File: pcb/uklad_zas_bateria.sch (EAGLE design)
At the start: 32 parts

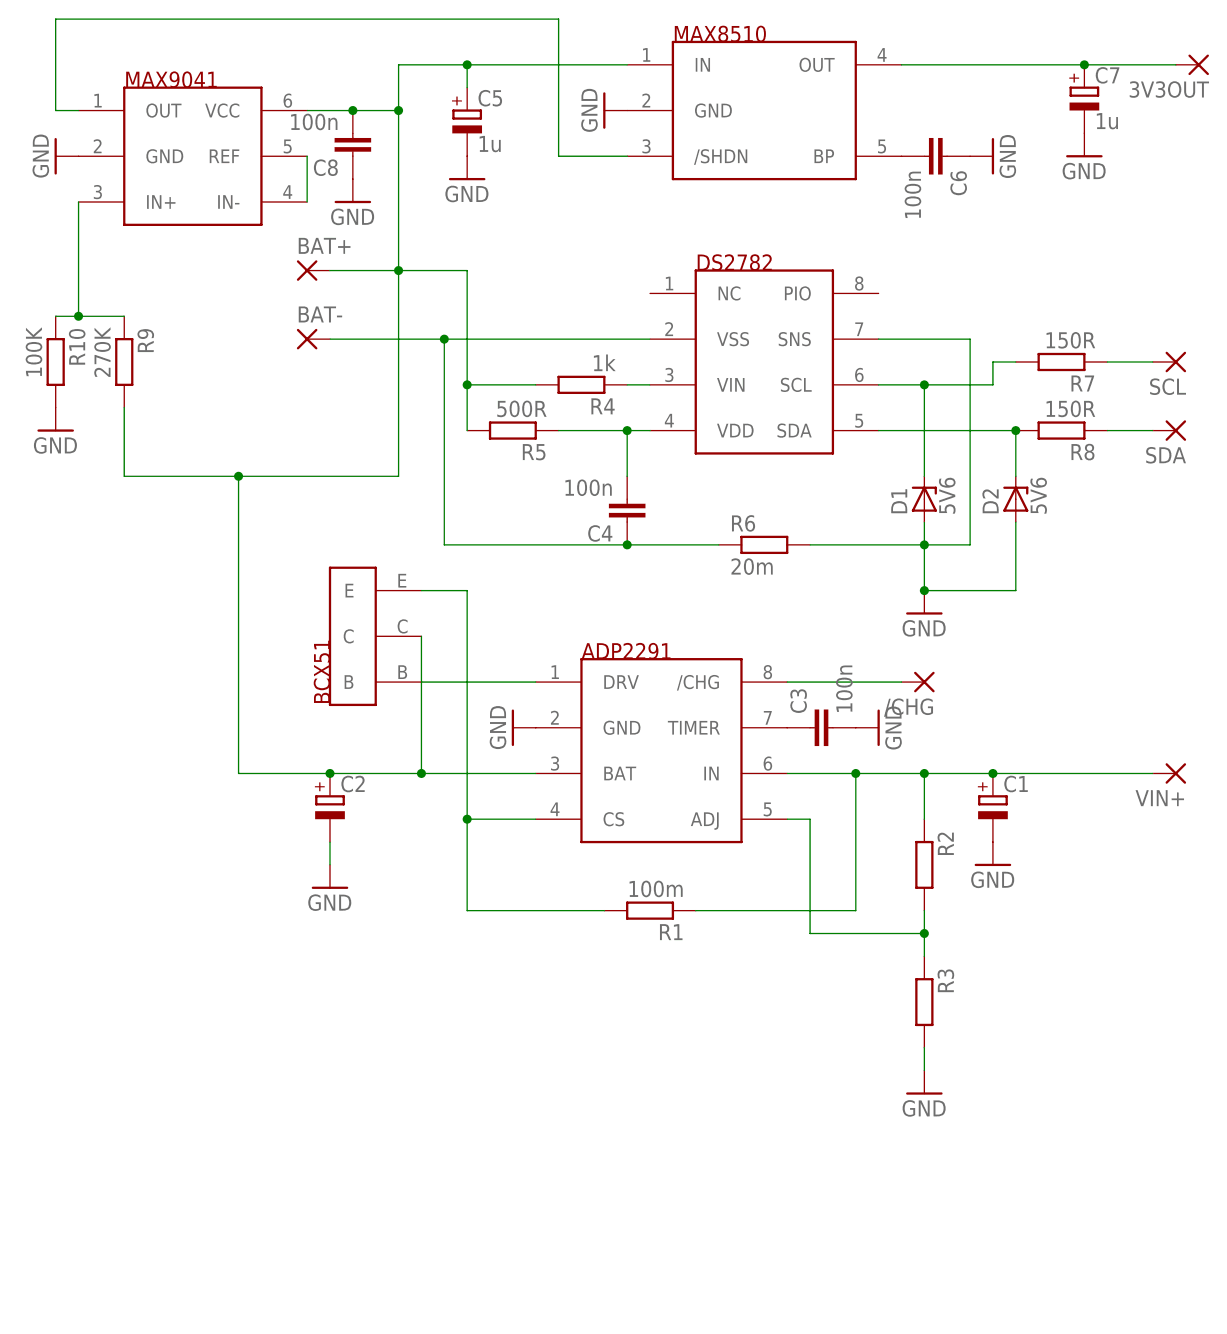
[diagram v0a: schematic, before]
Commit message: dodanie worda z magisterką gdzie pisze na bierząco, update kosztorysu, nowe bordy
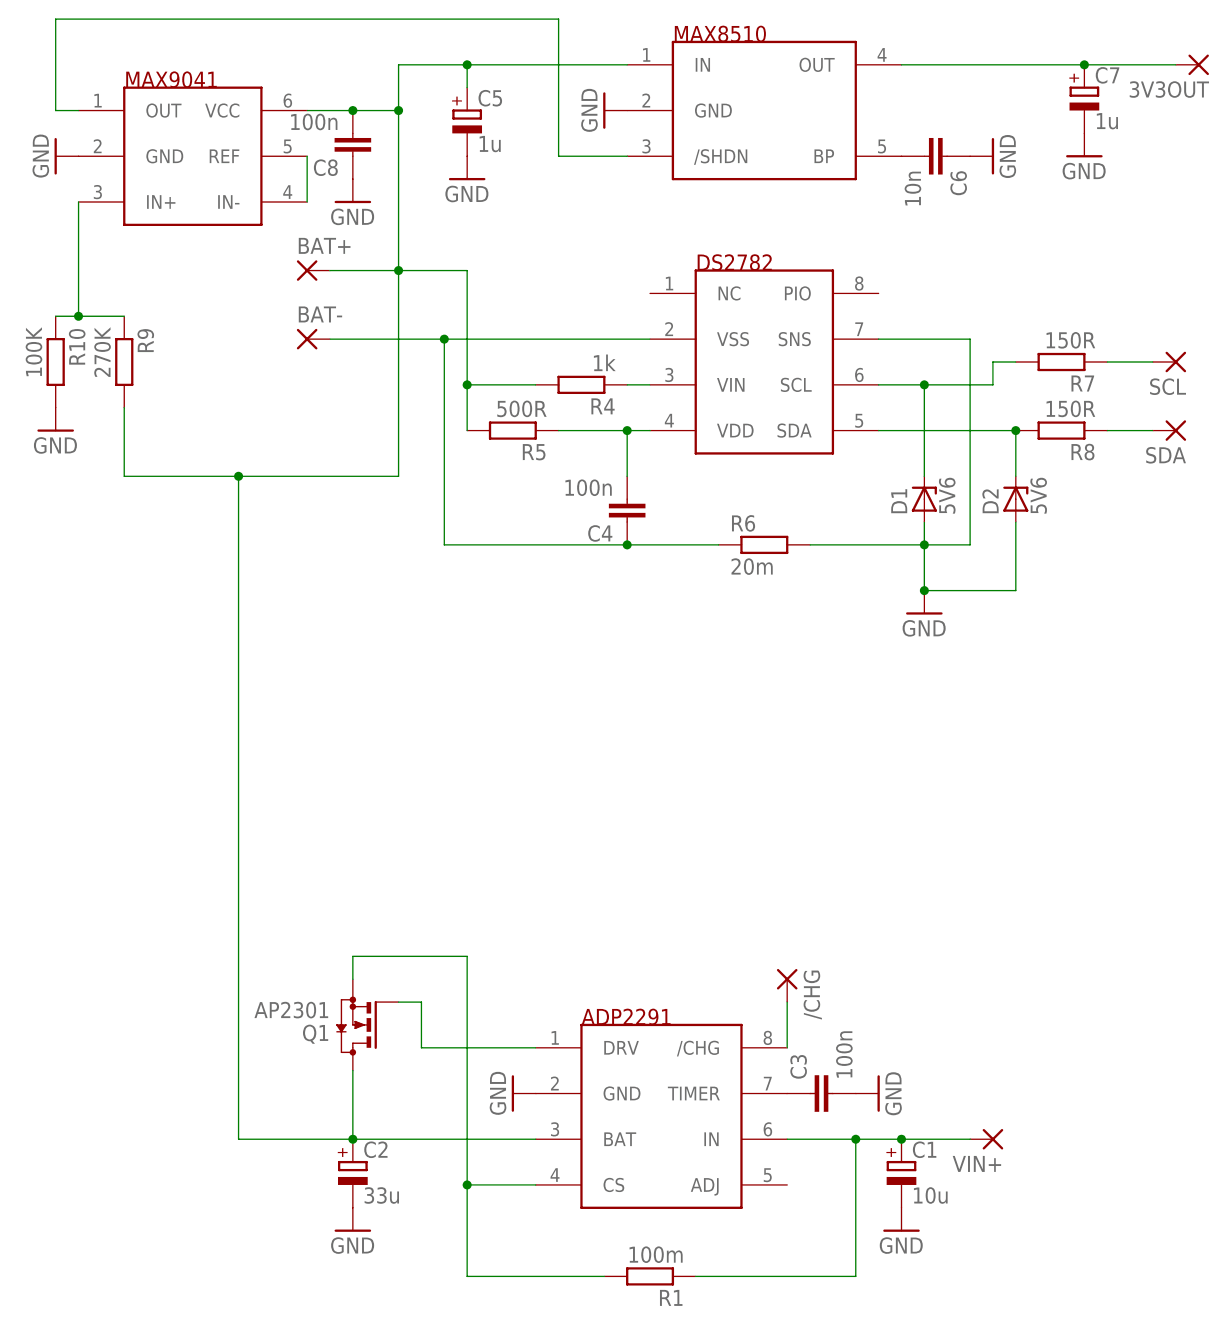
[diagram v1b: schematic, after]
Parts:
- removed R2, R3: (no value), resistor:R-EU_M0805
- removed U$2: BCX51, ref-packages:BCX51
- added Q1: AP2301, transistor-small-signal:BSS123
- C1: value (none) -> 10u
- C2: value (none) -> 33u
- C6: value 100n -> 10n; device rcl:C-EUC0805 -> rcl:C-EUC0603
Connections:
- removed net N$7: R2.2, R3.1, U$1.ADJ
- net GND: no longer R3.2
- net N$1: now also Q1.G; no longer U$2.B
- net N$19: now also Q1.D; no longer U$2.C
- net N$2: now also Q1.S; no longer U$2.E
- net N$3: no longer R2.1
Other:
- moved on the sheet: /CHG, C1, C2, C3, R1, VIN+
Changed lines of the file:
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@@
 <parts>
 <part name="U$1" library="ref-packages" deviceset="ADP2291" device=""/>
-<part name="U$2" library="ref-packages" deviceset="BCX51" device=""/>
 <part name="R1" library="rcl" deviceset="R-EU_" device="0207/10" value="100m"/>
-<part name="C1" library="rcl" deviceset="CPOL-EU" device="E2-5"/>
-<part name="C2" library="rcl" deviceset="CPOL-EU" device="E2-5"/>
+<part name="C1" library="rcl" deviceset="CPOL-EU" device="E2-5" value="10u"/>
+<part name="C2" library="rcl" deviceset="CPOL-EU" device="E2-5" value="33u"/>
 <part name="GND1" library="supply1" deviceset="GND" device=""/>
 <part name="GND2" library="supply1" deviceset="GND" device=""/>
 <part name="GND4" library="supply1" deviceset="GND" device=""/>
-<part name="R2" library="resistor" deviceset="R-EU_" device="M0805"/>
-<part name="R3" library="resistor" deviceset="R-EU_" device="M0805"/>
-<part name="GND3" library="supply1" deviceset="GND" device=""/>
 <part name="/CHG" library="wirepad" deviceset="2,54/0,8" device=""/>
 <part name="C3" library="rcl" deviceset="C-EU" device="C0805" value="100n"/>
@@
 <part name="C7" library="rcl" deviceset="CPOL-EU" device="E2-5" value="1u"/>
 <part name="GND10" library="supply1" deviceset="GND" device=""/>
-<part name="C6" library="rcl" deviceset="C-EU" device="C0805" value="100n"/>
+<part name="C6" library="rcl" deviceset="C-EU" device="C0603" value="10n"/>
 <part name="U$5" library="ref-packages" deviceset="MAX9041" device=""/>
 <part name="GND11" library="supply1" deviceset="GND" device=""/>
@@
 <part name="C8" library="rcl" deviceset="C-EU" device="C0805" value="100n"/>
 <part name="GND13" library="supply1" deviceset="GND" device=""/>
+<part name="Q1" library="transistor-small-signal" deviceset="BSS123" device="" value="AP2301"/>
 </parts>
 <sheets>
@@
 </plain>
 <instances>
-<instance part="U$1" gate="G$1" x="-81.28" y="27.94"/>
-<instance part="U$2" gate="G$1" x="-114.3" y="40.64" rot="R90"/>
-<instance part="R1" gate="G$1" x="-81.28" y="10.16" rot="R180"/>
-<instance part="C1" gate="G$1" x="-43.18" y="22.86"/>
-<instance part="C2" gate="G$1" x="-116.84" y="22.86"/>
-<instance part="GND1" gate="1" x="-116.84" y="12.7"/>
-<instance part="GND2" gate="1" x="-43.18" y="15.24"/>
-<instance part="GND4" gate="1" x="-96.52" y="30.48" rot="R270"/>
-<instance part="R2" gate="G$1" x="-50.8" y="15.24" rot="R270"/>
-<instance part="R3" gate="G$1" x="-50.8" y="0" rot="R270"/>
-<instance part="GND3" gate="1" x="-50.8" y="-10.16"/>
-<instance part="/CHG" gate="P" x="-50.8" y="35.56" rot="R180"/>
-<instance part="C3" gate="G$1" x="-63.5" y="30.48" rot="R90"/>
-<instance part="GND5" gate="1" x="-55.88" y="30.48" rot="R90"/>
-<instance part="VIN+" gate="P" x="-22.86" y="25.4" rot="R180"/>
+<instance part="U$1" gate="G$1" x="-81.28" y="-12.7"/>
+<instance part="R1" gate="G$1" x="-81.28" y="-30.48" rot="R180"/>
+<instance part="C1" gate="G$1" x="-53.34" y="-17.78"/>
+<instance part="C2" gate="G$1" x="-114.3" y="-17.78"/>
+<instance part="GND1" gate="1" x="-114.3" y="-25.4"/>
+<instance part="GND2" gate="1" x="-53.34" y="-25.4"/>
+<instance part="GND4" gate="1" x="-96.52" y="-10.16" rot="R270"/>
+<instance part="/CHG" gate="P" x="-66.04" y="2.54" rot="R270"/>
+<instance part="C3" gate="G$1" x="-63.5" y="-10.16" rot="R90"/>
+<instance part="GND5" gate="1" x="-55.88" y="-10.16" rot="R90"/>
+<instance part="VIN+" gate="P" x="-43.18" y="-15.24" rot="R180"/>
 <instance part="U$3" gate="G$1" x="-68.58" y="71.12"/>
 <instance part="C4" gate="G$1" x="-83.82" y="53.34" rot="R180"/>
@@
 <instance part="C8" gate="G$1" x="-114.3" y="93.98" rot="R180"/>
 <instance part="GND13" gate="1" x="-114.3" y="88.9"/>
+<instance part="Q1" gate="G$1" x="-114.3" y="-2.54" rot="R180"/>
 </instances>
 <busses>
 </busses>
 <nets>
-<net name="N$1" class="0">
-<segment>
-<pinref part="U$2" gate="G$1" pin="B"/>
-<wire x1="-93.98" y1="35.56" x2="-106.68" y2="35.56" width="0.1524" layer="91"/>
-<pinref part="U$1" gate="G$1" pin="DRV"/>
-</segment>
-</net>
 <net name="N$2" class="0">
 <segment>
 <pinref part="U$1" gate="G$1" pin="CS"/>
-<wire x1="-93.98" y1="20.32" x2="-101.6" y2="20.32" width="0.1524" layer="91"/>
-<wire x1="-101.6" y1="20.32" x2="-101.6" y2="45.72" width="0.1524" layer="91"/>
-<pinref part="U$2" gate="G$1" pin="E"/>
-<wire x1="-101.6" y1="45.72" x2="-106.68" y2="45.72" width="0.1524" layer="91"/>
-<wire x1="-101.6" y1="20.32" x2="-101.6" y2="10.16" width="0.1524" layer="91"/>
-<junction x="-101.6" y="20.32"/>
+<wire x1="-93.98" y1="-20.32" x2="-101.6" y2="-20.32" width="0.1524" layer="91"/>
+<wire x1="-101.6" y1="-20.32" x2="-101.6" y2="5.08" width="0.1524" layer="91"/>
+<wire x1="-101.6" y1="-20.32" x2="-101.6" y2="-30.48" width="0.1524" layer="91"/>
+<junction x="-101.6" y="-20.32"/>
 <pinref part="R1" gate="G$1" pin="2"/>
-<wire x1="-101.6" y1="10.16" x2="-86.36" y2="10.16" width="0.1524" layer="91"/>
+<wire x1="-101.6" y1="-30.48" x2="-86.36" y2="-30.48" width="0.1524" layer="91"/>
+<pinref part="Q1" gate="G$1" pin="S"/>
+<wire x1="-101.6" y1="5.08" x2="-114.3" y2="5.08" width="0.1524" layer="91"/>
+<wire x1="-114.3" y1="5.08" x2="-114.3" y2="2.54" width="0.1524" layer="91"/>
 </segment>
 </net>
@@
 <segment>
 <pinref part="R1" gate="G$1" pin="1"/>
-<wire x1="-76.2" y1="10.16" x2="-58.42" y2="10.16" width="0.1524" layer="91"/>
-<wire x1="-58.42" y1="10.16" x2="-58.42" y2="25.4" width="0.1524" layer="91"/>
+<wire x1="-76.2" y1="-30.48" x2="-58.42" y2="-30.48" width="0.1524" layer="91"/>
+<wire x1="-58.42" y1="-30.48" x2="-58.42" y2="-15.24" width="0.1524" layer="91"/>
 <pinref part="U$1" gate="G$1" pin="IN"/>
-<wire x1="-58.42" y1="25.4" x2="-66.04" y2="25.4" width="0.1524" layer="91"/>
-<wire x1="-58.42" y1="25.4" x2="-50.8" y2="25.4" width="0.1524" layer="91"/>
-<junction x="-58.42" y="25.4"/>
+<wire x1="-58.42" y1="-15.24" x2="-66.04" y2="-15.24" width="0.1524" layer="91"/>
+<junction x="-58.42" y="-15.24"/>
 <pinref part="C1" gate="G$1" pin="+"/>
-<wire x1="-50.8" y1="25.4" x2="-43.18" y2="25.4" width="0.1524" layer="91"/>
-<wire x1="-43.18" y1="25.4" x2="-25.4" y2="25.4" width="0.1524" layer="91"/>
-<junction x="-43.18" y="25.4"/>
-<pinref part="R2" gate="G$1" pin="1"/>
-<wire x1="-50.8" y1="20.32" x2="-50.8" y2="25.4" width="0.1524" layer="91"/>
-<junction x="-50.8" y="25.4"/>
+<wire x1="-58.42" y1="-15.24" x2="-53.34" y2="-15.24" width="0.1524" layer="91"/>
+<wire x1="-53.34" y1="-15.24" x2="-45.72" y2="-15.24" width="0.1524" layer="91"/>
+<junction x="-53.34" y="-15.24"/>
 <pinref part="VIN+" gate="P" pin="P"/>
 </segment>
@@
 <segment>
 <pinref part="U$1" gate="G$1" pin="/CHG"/>
-<wire x1="-66.04" y1="35.56" x2="-53.34" y2="35.56" width="0.1524" layer="91"/>
+<wire x1="-66.04" y1="-5.08" x2="-66.04" y2="0" width="0.1524" layer="91"/>
 <pinref part="/CHG" gate="P" pin="P"/>
 </segment>
@@
 <pinref part="C2" gate="G$1" pin="-"/>
 <pinref part="GND1" gate="1" pin="GND"/>
-<wire x1="-116.84" y1="17.78" x2="-116.84" y2="15.24" width="0.1524" layer="91"/>
 </segment>
 <segment>
@@
 <pinref part="U$1" gate="G$1" pin="GND"/>
 <pinref part="GND4" gate="1" pin="GND"/>
-</segment>
-<segment>
-<pinref part="R3" gate="G$1" pin="2"/>
-<pinref part="GND3" gate="1" pin="GND"/>
-<wire x1="-50.8" y1="-5.08" x2="-50.8" y2="-7.62" width="0.1524" layer="91"/>
 </segment>
 <segment>
@@
 </segment>
 </net>
-<net name="N$7" class="0">
-<segment>
-<pinref part="R3" gate="G$1" pin="1"/>
-<pinref part="R2" gate="G$1" pin="2"/>
-<wire x1="-50.8" y1="5.08" x2="-50.8" y2="7.62" width="0.1524" layer="91"/>
-<pinref part="U$1" gate="G$1" pin="ADJ"/>
-<wire x1="-50.8" y1="7.62" x2="-50.8" y2="10.16" width="0.1524" layer="91"/>
-<wire x1="-66.04" y1="20.32" x2="-63.5" y2="20.32" width="0.1524" layer="91"/>
-<wire x1="-50.8" y1="7.62" x2="-63.5" y2="7.62" width="0.1524" layer="91"/>
-<wire x1="-63.5" y1="7.62" x2="-63.5" y2="20.32" width="0.1524" layer="91"/>
-<junction x="-50.8" y="7.62"/>
-</segment>
-</net>
 <net name="N$6" class="0">
 <segment>
@@
 <net name="N$19" class="0">
 <segment>
-<wire x1="-106.68" y1="25.4" x2="-116.84" y2="25.4" width="0.1524" layer="91"/>
 <pinref part="U$1" gate="G$1" pin="BAT"/>
-<wire x1="-116.84" y1="25.4" x2="-127" y2="25.4" width="0.1524" layer="91"/>
-<wire x1="-93.98" y1="25.4" x2="-106.68" y2="25.4" width="0.1524" layer="91"/>
-<junction x="-106.68" y="25.4"/>
-<pinref part="U$2" gate="G$1" pin="C"/>
-<wire x1="-106.68" y1="40.64" x2="-106.68" y2="25.4" width="0.1524" layer="91"/>
+<wire x1="-114.3" y1="-15.24" x2="-127" y2="-15.24" width="0.1524" layer="91"/>
+<wire x1="-93.98" y1="-15.24" x2="-114.3" y2="-15.24" width="0.1524" layer="91"/>
 <pinref part="C2" gate="G$1" pin="+"/>
-<junction x="-116.84" y="25.4"/>
+<junction x="-114.3" y="-15.24"/>
 <pinref part="U$4" gate="G$1" pin="IN"/>
 <pinref part="C5" gate="G$1" pin="+"/>
@@
 <junction x="-114.3" y="99.06"/>
 <wire x1="-127" y1="58.42" x2="-109.22" y2="58.42" width="0.1524" layer="91"/>
-<wire x1="-127" y1="25.4" x2="-127" y2="58.42" width="0.1524" layer="91"/>
+<wire x1="-127" y1="-15.24" x2="-127" y2="58.42" width="0.1524" layer="91"/>
 <junction x="-127" y="58.42"/>
-</segment>
-</net>
+<pinref part="Q1" gate="G$1" pin="D"/>
+<wire x1="-114.3" y1="-7.62" x2="-114.3" y2="-15.24" width="0.1524" layer="91"/>
+</segment>
+</net>
+<net name="N$1" class="0">
+<segment>
+<pinref part="U$1" gate="G$1" pin="DRV"/>
+<wire x1="-93.98" y1="-5.08" x2="-106.68" y2="-5.08" width="0.1524" layer="91"/>
+<wire x1="-106.68" y1="-5.08" x2="-106.68" y2="0" width="0.1524" layer="91"/>
+<pinref part="Q1" gate="G$1" pin="G"/>
+<wire x1="-106.68" y1="0" x2="-109.22" y2="0" width="0.1524" layer="91"/>
+</segment>
+</net>
